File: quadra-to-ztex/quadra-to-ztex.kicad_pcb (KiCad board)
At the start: 4 copper layers, 100 x 100 mm, 31 parts, among them IC1 74CB3T16211DGGR, IC2 74CB3T16211DGGR, IC3 74CB3T16211DGGR, IC4 74CB3T16211DGGR, J1 Conn_02x07_Odd_Even, J2 10029449-111RLF (HDMI A), J3 A2541HWR-2x6P (Pmod 2x6 F R), U1 TPD12S016PWR, U14 8807-140-170LH

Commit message: length tuning
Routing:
- net PMOD-1112-: track 50.7 -> 71.4 mm
- net PMOD-910-: track 56.9 -> 74.6 mm
- net PMOD-1112+: track 53.5 -> 68.6 mm
- net PMOD-910+: track 59.7 -> 72.5 mm
- net PMOD-78-: track 63.0 -> 73.2 mm
- net PMOD-78+: track 65.8 -> 73.2 mm
- net HDMI_D0+: track 24.9 -> 31.8 mm
- net HDMI_D0-: track 24.4 -> 30.0 mm
- net HDMI_D2+: track 30.2 -> 34.8 mm
- net HDMI_D2-: track 29.7 -> 33.7 mm
- net HDMI_CLK-: track 31.0 -> 33.5 mm
- net HDMI_CLK+: track 30.5 -> 31.9 mm
- net PMOD-56-: track 69.2 -> 70.2 mm
- net HDMI_D1-: track 35.9 -> 36.5 mm
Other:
- board text added: "104"
- board text added: "11"
- board text added: "114"
- board text added: "124"
- board text added: "2"
- board text added: "21"
- board text added: "29"
- board text added: "3"
- board text added: "39"
- board text added: "49"
- board text added: "59"
- board text added: "64"
- board text added: "71"
- board text added: "72"
- board text added: "86"
- board text added: "91"
- board text added: "94"
- board text added: "Power"

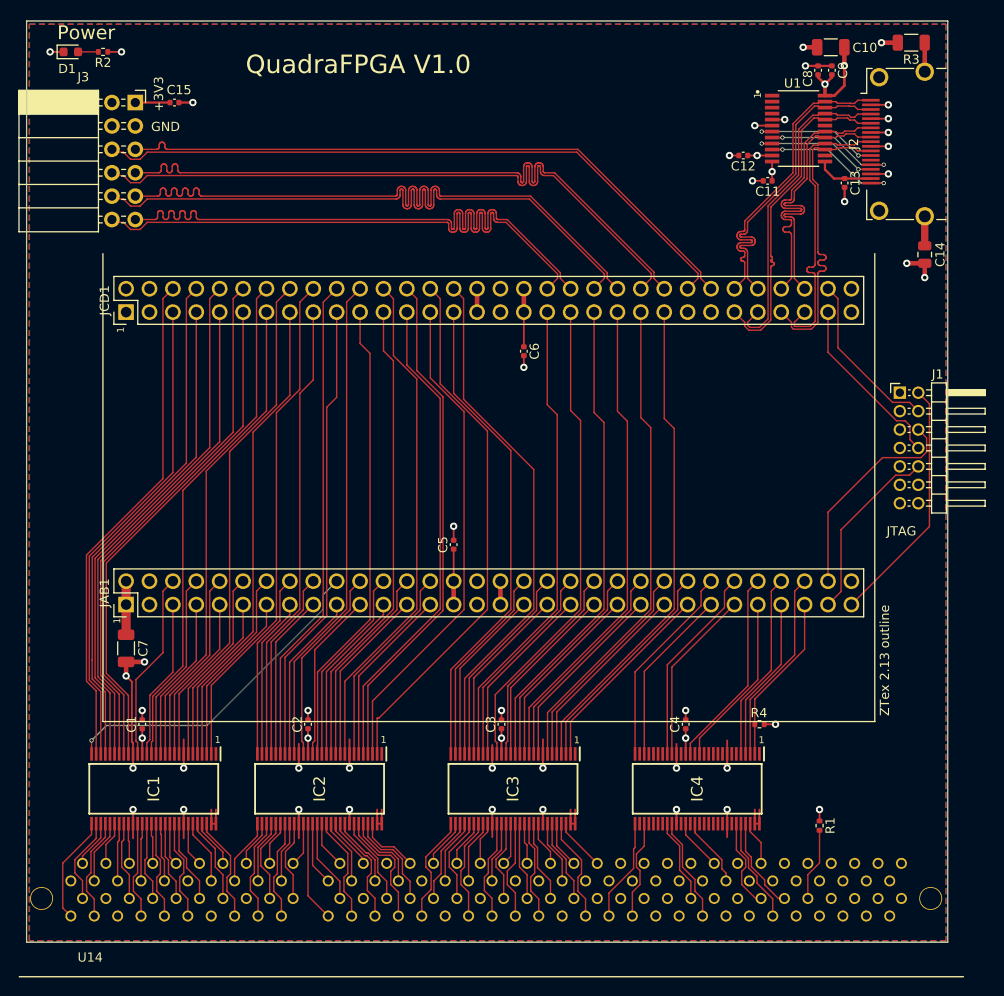
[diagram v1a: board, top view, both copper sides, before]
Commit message: remove memreset, add busmastering (?)
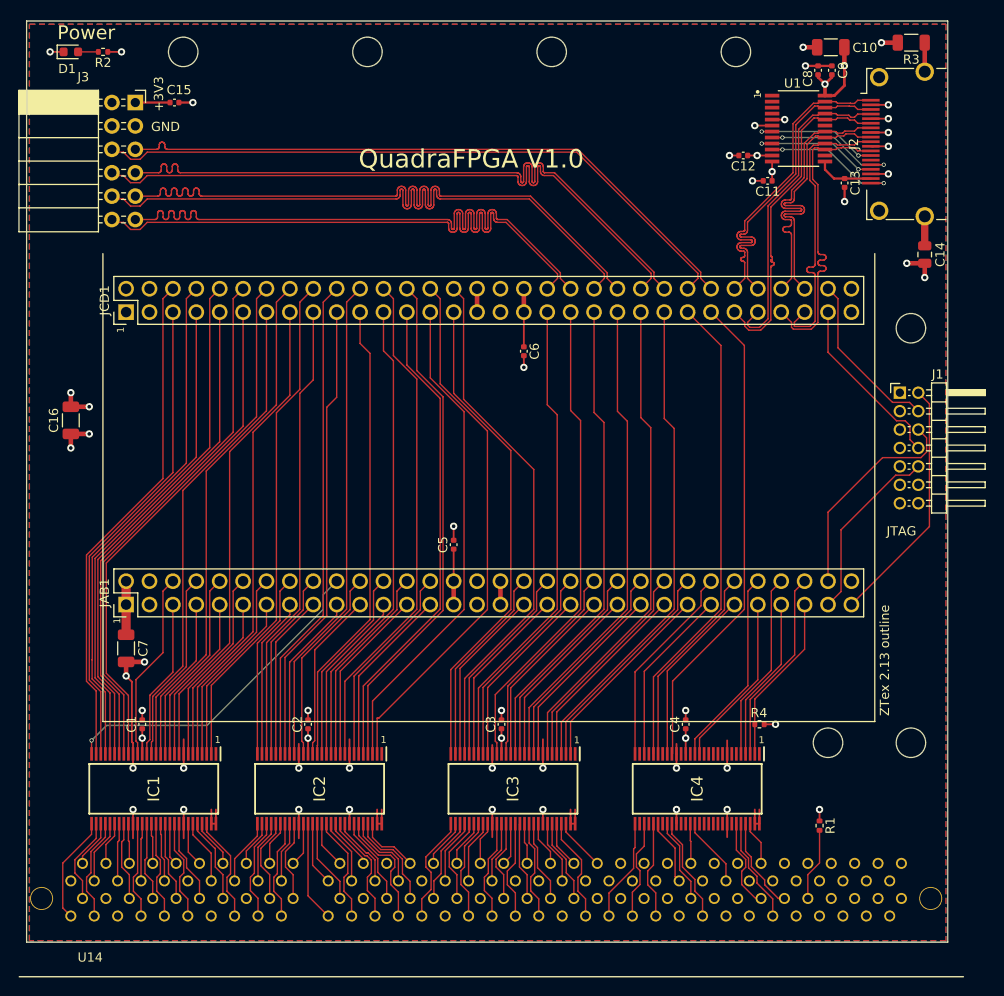
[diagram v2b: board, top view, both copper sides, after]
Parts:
- added C16: 47uF 10V+, Capacitor_SMD:C_1206_3216Metric, F.Cu at (100.0, 100.0)
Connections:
- IC4 pad 15: (no net) -> ~BB_3V3
- IC4 pad 16: ~MEMRESET_3V3 -> (no net)
- IC4 pad 23: (no net) -> ~BR_40SLOT_3V3
- IC4 pad 24: (no net) -> ~BG_40SLOT_3V3
- IC4 pad 33: (no net) -> ~BG_40SLOT
- IC4 pad 34: (no net) -> ~BR_40SLOT
- IC4 pad 40: ~MEMRESET -> (no net)
- IC4 pad 41: (no net) -> ~BB
- JAB1 pad 53: TT1_3V3 -> TT0_3V3
- JAB1 pad 54: TT0_3V3 -> ~BR_40SLOT_3V3
- JAB1 pad 56: ~MEMRESET_3V3 -> ~BB_3V3
- JCD1 pad 49: (no net) -> ~BG_40SLOT_3V3
- JCD1 pad 51: (no net) -> TT1_3V3
- U14 pad 119: (no net) -> ~BG_40SLOT
- U14 pad 51: (no net) -> ~BR_40SLOT
- U14 pad 52: (no net) -> ~BB
- U14 pad 54: ~MEMRESET -> (no net)
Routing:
- net ~BG_40SLOT_3V3: track 0.00 -> 52.5 mm
- net TT1_3V3: track 19.0 -> 52.7 mm
- net ~BR_40SLOT_3V3: track 0.00 -> 22.2 mm
- net ~MEMRESET_3V3: track 21.8 -> 0.00 mm
- net ~BB_3V3: track 0.00 -> 21.6 mm
- net ~BG_40SLOT: track 0.00 -> 10.6 mm
- net ~BR_40SLOT: track 0.00 -> 7.16 mm
- net ~MEMRESET: track 5.59 -> 0.00 mm
- net ~BB: track 0.00 -> 4.33 mm
- net GND: track 105.9 -> 109.4 mm, vias 41 -> 43
- net +3V3: track 48.9 -> 52.5 mm, vias 10 -> 12
- net TT0_3V3: track 21.8 -> 19.3 mm
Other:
- outline, holes or cut-outs redrawn

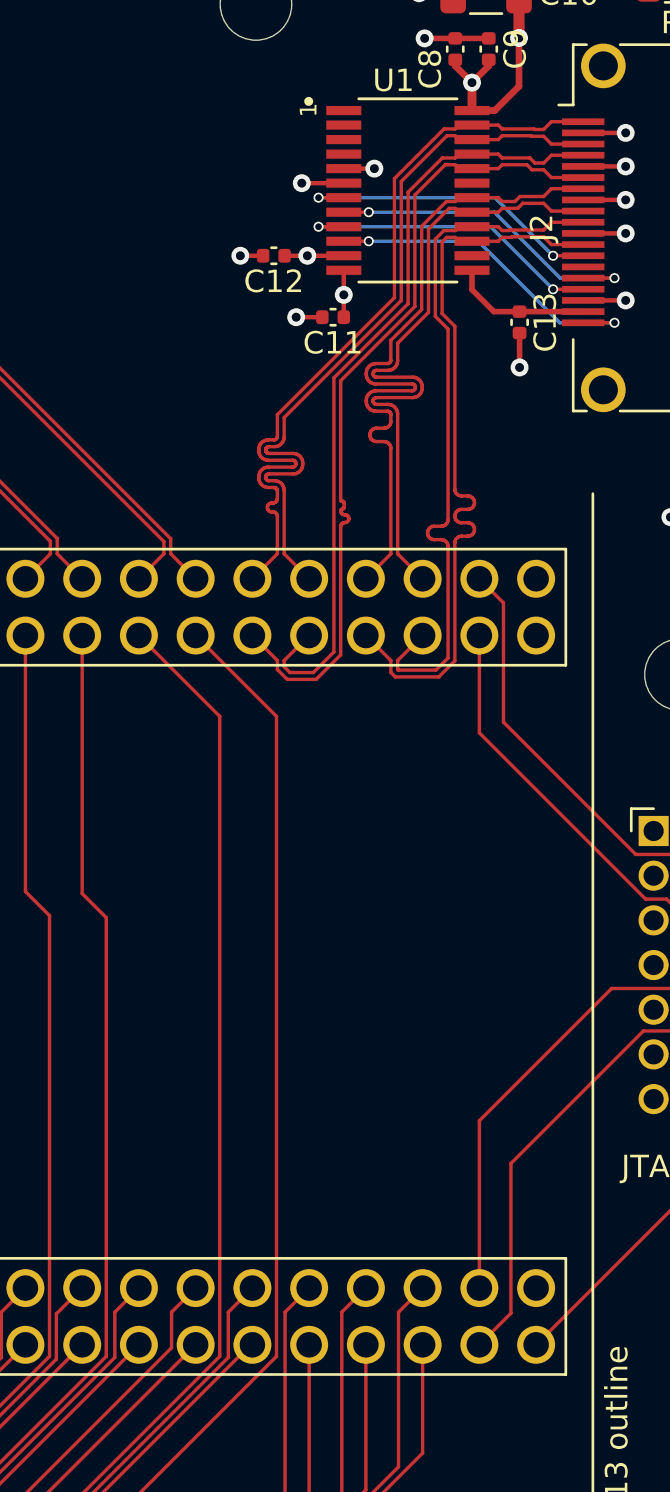
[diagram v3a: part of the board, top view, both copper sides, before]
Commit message: rewire to avoid p/n conflicts
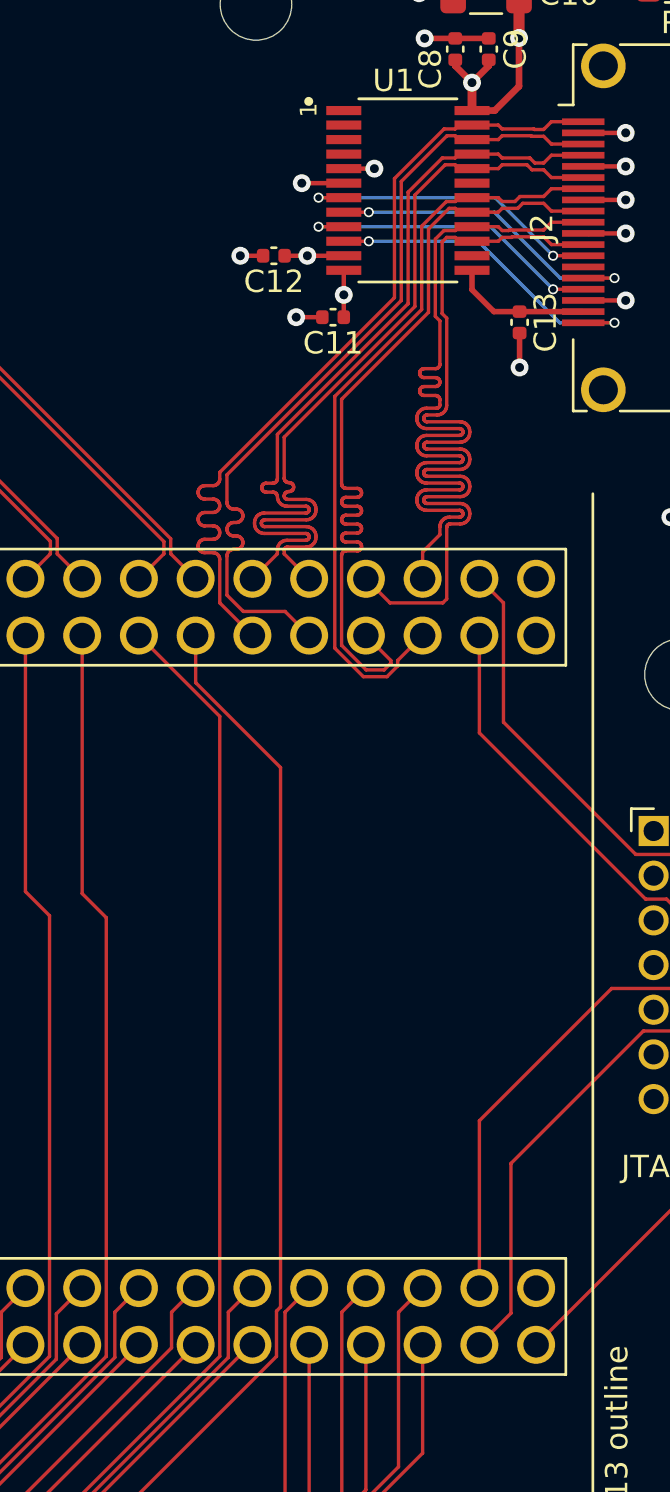
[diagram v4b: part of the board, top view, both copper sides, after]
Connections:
- JCD1 pad 53: HDMI_D1- -> HDMI_D2+
- JCD1 pad 54: HDMI_D2+ -> HDMI_D1+
- JCD1 pad 55: HDMI_D1+ -> HDMI_D2-
- JCD1 pad 56: HDMI_D2- -> HDMI_D1-
- JCD1 pad 57: HDMI_CLK- -> HDMI_D0-
- JCD1 pad 58: HDMI_D0+ -> HDMI_CLK-
- JCD1 pad 59: HDMI_CLK+ -> HDMI_D0+
- JCD1 pad 60: HDMI_D0- -> HDMI_CLK+
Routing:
- net HDMI_D0-: track 30.0 -> 38.2 mm
- net HDMI_CLK+: track 31.9 -> 39.9 mm
- net HDMI_CLK-: track 33.5 -> 41.1 mm
- net HDMI_D2-: track 33.7 -> 37.3 mm
- net HDMI_D2+: track 34.8 -> 38.2 mm
- net HDMI_D0+: track 31.8 -> 33.9 mm
- net HDMI_D1+: track 35.4 -> 36.8 mm
- net HDMI_D1-: track 36.5 -> 35.8 mm

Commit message: fix lengths
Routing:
- net HDMI_CLK+: track 39.9 -> 31.9 mm
- net HDMI_CLK-: track 41.1 -> 33.8 mm
- net PMOD-1112-: track 71.4 -> 68.6 mm
- net HDMI_D0-: track 38.2 -> 35.6 mm
- net PMOD-1112+: track 68.6 -> 66.6 mm
- net PMOD-910-: track 74.6 -> 72.8 mm
- net PMOD-78+: track 73.2 -> 74.6 mm
- net PMOD-910+: track 72.5 -> 71.4 mm
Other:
- board text removed: "QuadraFPGA V1.0"

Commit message: logo
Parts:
- added GRAPHIC1: LogoLitex, For_SeeedStudio:litex_logo, F.Cu at (152.2, 75.0)
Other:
- board text added: "QuadraFPGA V1.0"

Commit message: oups A5
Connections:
- U14 pad 75: GND -> A5
- U14 pad 76: A5 -> GND
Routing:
- net A5: track 8.55 -> 10.7 mm

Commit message: regen
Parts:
- IC1, IC2, IC3, IC4: footprint For_SeeedStudio:SOP50P810X120-56N -> SOP50P810X120-56N
